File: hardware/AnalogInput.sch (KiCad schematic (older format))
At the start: 74 parts

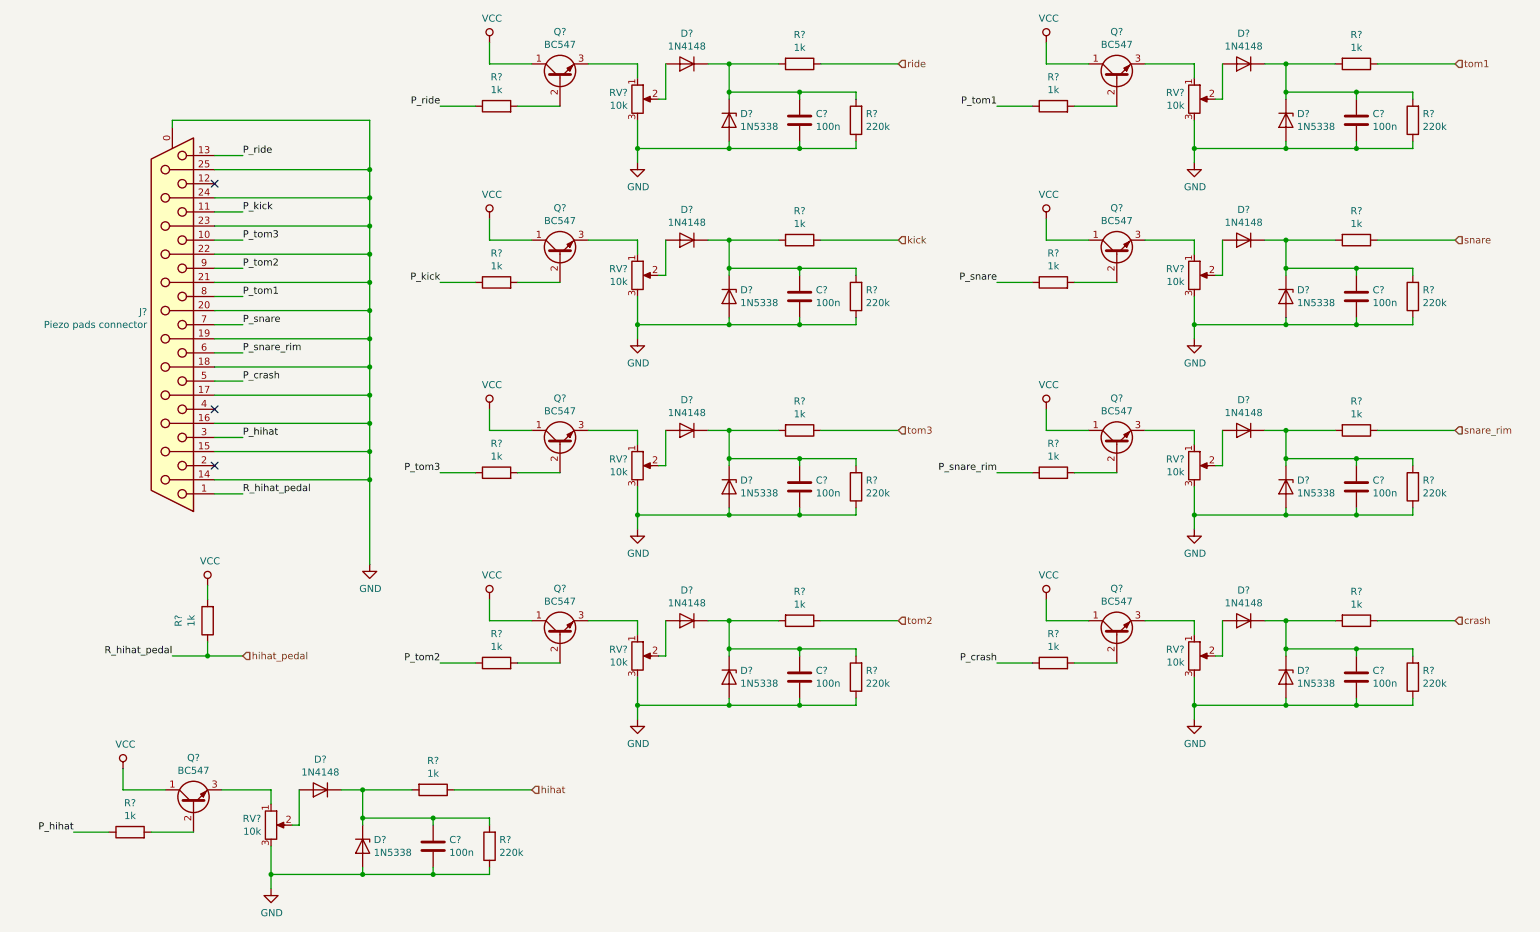
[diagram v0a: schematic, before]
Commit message: Update board
simplify analog input
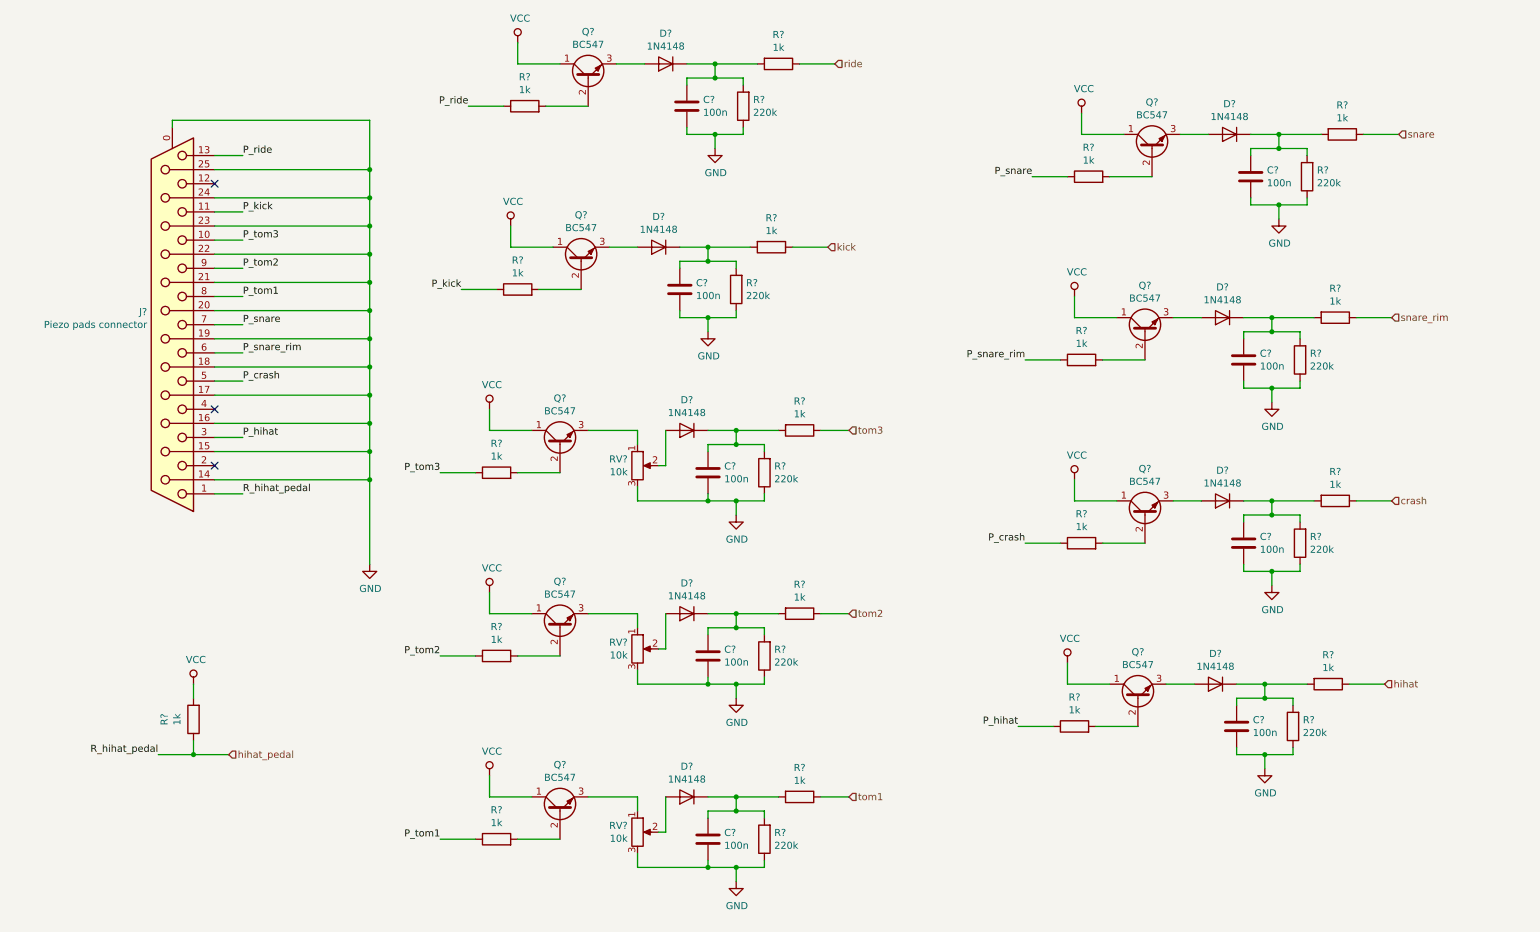
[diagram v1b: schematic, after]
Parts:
- removed C? (x7): 100n, symbol Device:C
- removed D? (x9): 1N5338, symbol Device:D_Zener
- removed D? (x7): 1N4148, Diode_THT:D_DO-35_SOD27_P7.62mm_Horizontal, symbol Diode:1N4148
- removed Q? (x7): BC547, Package_TO_SOT_THT:TO-92_Inline, symbol Transistor_BJT:BC547
- removed R? (x14): 1k, symbol Device:R
- removed R? (x7): 220k, symbol Device:R
- removed RV? (x8): 10k, symbol Device:R_POT
- added C? (x7): 100n, symbol Device:C
- added D? (x7): 1N4148, Diode_THT:D_DO-35_SOD27_P7.62mm_Horizontal, symbol Diode:1N4148
- added Q? (x7): BC547, Package_TO_SOT_THT:TO-92_Inline, symbol Transistor_BJT:BC547
- added R? (x14): 1k, symbol Device:R
- added R? (x7): 220k, symbol Device:R
- added RV? (x2): 10k, symbol Device:R_POT
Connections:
- net GND: now also C?.2, C?.2, C?.2, C?.2, C?.2, C?.2, C?.2, R?.1, R?.1, R?.1, R?.1, R?.1, R?.1, R?.1, RV?.3, RV?.3
- net P_crash: now also R?.1
- net P_hihat: now also R?.1
- net P_kick: now also R?.1
- net P_snare: now also R?.1
- net P_snare_rim: now also R?.1
- net P_tom1: now also R?.1
- net P_tom2: now also R?.1
- net VCC: now also Q?.1 (C), Q?.1 (C), Q?.1 (C), Q?.1 (C), Q?.1 (C), Q?.1 (C), Q?.1 (C)
- net crash: now also R?.1
- net hihat: now also R?.1
- net kick: now also R?.1
- net snare: now also R?.1
- net snare_rim: now also R?.1
- net tom1: now also R?.1
- net tom2: now also R?.1
- net at Q?.3 (E): now also D?.2 (A)
- new net: Q?.2 (B), R?.2 (x7)
- new net: D?.2 (A), Q?.3 (E) (x5)
- new net: C?.1, D?.1 (K), R?.2, R?.2 (x7)
- new net: D?.2 (A), RV?.2 (x2)
- new net: Q?.3 (E), RV?.1 (x2)
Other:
- moved on the sheet: C?, D?, Q?, R?
